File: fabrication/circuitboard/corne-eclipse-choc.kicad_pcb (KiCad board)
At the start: 2 copper layers, 275.5 x 105.6 mm, 178 parts, among them J2 OLED, J4 OLED, SW1 SW_Choc_v1v2_HS, SW10 SW_Choc_v1v2_HS, SW11 SW_Choc_v1v2_HS, SW12 SW_Choc_v1v2_HS, SW13 SW_Choc_v1v2_HS, SW14 SW_Choc_v1v2_HS, SW15 SW_Choc_v1v2_HS, SW16 SW_Choc_v1v2_HS, SW17 SW_Choc_v1v2_HS, SW18 SW_Choc_v1v2_HS, SW2 SW_Choc_v1v2_HS, SW20 SW_Choc_v1v2_HS, SW21 SW_Choc_v1v2_HS, SW22 SW_Choc_v1v2_HS, SW23 SW_Choc_v1v2_HS, SW24 SW_Choc_v1v2_HS, SW25 SW_Choc_v1v2_HS, SW26 SW_Choc_v1v2_HS, SW27 SW_Choc_v1v2_HS, SW28 SW_Choc_v1v2_HS, SW29 SW_Choc_v1v2_HS, SW3 SW_Choc_v1v2_HS, SW30 SW_Choc_v1v2_HS, SW31 SW_Choc_v1v2_HS, SW32 SW_Choc_v1v2_HS, SW33 SW_Choc_v1v2_HS, SW34 SW_Choc_v1v2_HS, SW35 SW_Choc_v1v2_HS, SW36 SW_Choc_v1v2_HS, SW37 SW_Choc_v1v2_HS, SW38 SW_Choc_v1v2_HS, SW39 SW_Choc_v1v2_HS, SW4 SW_Choc_v1v2_HS, SW40 SW_Choc_v1v2_HS, SW42 SW_Choc_v1v2_HS, SW43 SW_Choc_v1v2_HS, SW44 SW_Choc_v1v2_HS, SW5 SW_Choc_v1v2_HS, SW6 SW_Choc_v1v2_HS, SW7 SW_Choc_v1v2_HS, SW8 SW_Choc_v1v2_HS, SW9 SW_Choc_v1v2_HS, U1 nice!nano, U2 nice!nano

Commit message: wip: v3 mx+choc variants
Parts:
- added Q1: AO3401A, Package_TO_SOT_SMD:SOT-23, B.Cu at (123.6, 61.2)
- added Q2: AO3401A, Package_TO_SOT_SMD:SOT-23, B.Cu at (173.2, 61.2)
- added R1: 10k, Resistor_SMD:R_0402_1005Metric, B.Cu at (124.4, 64.0)
- added R2: 10k, Resistor_SMD:R_0402_1005Metric, B.Cu at (172.4, 64.0)
- ENC1, ENC2: value RotaryEncoder_Alps_EC12E-Switch_Vertical_H20mm -> ENC_SW_EC12_Choc; footprint Rotary_Encoder:RotaryEncoder_Alps_EC12E-Switch_Vertical_H20mm -> Corne Eclipse:ENC_SW_EC12_Choc_v1v2_HS_1u
- SW1, SW10, SW11, SW12, SW13, SW14, SW15, SW16, SW17, SW18, SW2, SW20, SW21, SW23, SW24, SW25, SW26, SW27, SW28, SW29, SW3, SW30, SW31, SW32, SW33, SW34, SW35, SW36, SW37, SW38, SW39, SW4, SW40, SW42, SW43, SW5, SW6, SW7, SW8, SW9: footprint corne-eclipse:SW_Choc_v1v2_HS_1u -> Corne Eclipse:SW_Choc_v1v2_HS_1u
- SW22, SW44: footprint corne-eclipse:SW_Choc_v1v2_HS_1.5u -> Corne Eclipse:SW_Choc_v1v2_HS_1.5u
- TP1, TP2: footprint corne-eclipse:Tenting_Puck -> Corne Eclipse:Tenting_Puck
- moved LED36 9.51 mm to (181.6, 65.7), turned to 180 degrees
- moved LED41 9.51 mm to (200.6, 63.3), turned to 180 degrees
- moved LED43 9.51 mm to (210.1, 82.9), turned to 180 degrees
- moved LED44 9.51 mm to (219.6, 60.9), turned to 180 degrees
- moved LED49 9.51 mm to (238.6, 63.3), turned to 180 degrees
- moved LED51 9.51 mm to (257.6, 68.0), turned to 180 degrees
- moved LED56 9.51 mm to (276.6, 68.0), turned to 180 degrees
- moved LED37 9.51 mm to (181.6, 46.7), turned to 180 degrees
- moved LED39 9.51 mm to (200.6, 25.3), turned to 180 degrees
- moved LED40 9.51 mm to (200.6, 44.3), turned to 180 degrees
- moved LED46 9.51 mm to (219.6, 22.9), turned to 180 degrees
- moved LED47 9.51 mm to (238.6, 25.3), turned to 180 degrees
- moved LED48 9.51 mm to (238.6, 44.3), turned to 180 degrees
- moved LED52 9.51 mm to (257.6, 49.0), turned to 180 degrees
- moved LED53 9.51 mm to (257.6, 30.0), turned to 180 degrees
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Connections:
- net Net-(U1-Pad14) renamed SPI_SCK
- net Net-(U2-Pad14) renamed SPI_SCK_r
- LED1 pad 1: VCC -> LED_PWR
- LED1 pad prev: led0-led1 -> LED
- LED10 pad 3: VCC -> LED_PWR
- LED11 pad 3: VCC -> LED_PWR
- LED12 pad 3: VCC -> LED_PWR
- LED13 pad 3: VCC -> LED_PWR
- LED14 pad 3: VCC -> LED_PWR
- LED15 pad 3: VCC -> LED_PWR
- LED16 pad 3: VCC -> LED_PWR
- LED17 pad 3: VCC -> LED_PWR
- LED18 pad 3: VCC -> LED_PWR
- LED19 pad 3: VCC -> LED_PWR
- LED2 pad 1: VCC -> LED_PWR
- LED20 pad 3: VCC -> LED_PWR
- LED21 pad 3: VCC -> LED_PWR
- LED23 pad 3: VCC -> LED_PWR
- LED24 pad 3: VCC -> LED_PWR
- LED25 pad 3: VCC -> LED_PWR
- LED26 pad 3: VCC -> LED_PWR
- LED27 pad 3: VCC -> LED_PWR
- LED28 pad 3: VCC -> LED_PWR
- LED29 pad 1: VDD -> LED_PWR_r
- LED3 pad 1: VCC -> LED_PWR
- LED30 pad 1: VDD -> LED_PWR_r
- LED31 pad 1: VDD -> LED_PWR_r
- LED32 pad 1: VDD -> LED_PWR_r
- LED33 pad 1: VDD -> LED_PWR_r
- LED33B pad 1: VDD -> LED_PWR_r
- LED35 pad 3: VDD -> LED_PWR_r
- LED36 pad 3: VDD -> LED_PWR_r
- LED37 pad 3: VDD -> LED_PWR_r
- LED38 pad 3: VDD -> LED_PWR_r
- LED39 pad 3: VDD -> LED_PWR_r
- LED4 pad 1: VCC -> LED_PWR
- LED40 pad 3: VDD -> LED_PWR_r
- LED41 pad 3: VDD -> LED_PWR_r
- LED42 pad 3: VDD -> LED_PWR_r
- LED43 pad 3: VDD -> LED_PWR_r
- LED44 pad 3: VDD -> LED_PWR_r
- LED45 pad 3: VDD -> LED_PWR_r
- LED46 pad 3: VDD -> LED_PWR_r
- LED47 pad 3: VDD -> LED_PWR_r
- LED48 pad 3: VDD -> LED_PWR_r
- LED49 pad 3: VDD -> LED_PWR_r
- LED5 pad 1: VCC -> LED_PWR
- LED51 pad 3: VDD -> LED_PWR_r
- LED52 pad 3: VDD -> LED_PWR_r
- LED53 pad 3: VDD -> LED_PWR_r
- LED54 pad 3: VDD -> LED_PWR_r
- LED55 pad 3: VDD -> LED_PWR_r
- LED56 pad 3: VDD -> LED_PWR_r
- LED6 pad 1: VCC -> LED_PWR
- LED7 pad 3: VCC -> LED_PWR
- LED8 pad 3: VCC -> LED_PWR
- LED9 pad 3: VCC -> LED_PWR
- U1 pad 13: Net-(U1-Pad13) -> EXT_PWR
- U2 pad 13: Net-(U2-Pad13) -> EXT_PWR_r
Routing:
- net GND: track 0.27 -> 536.8 mm, vias 0 -> 28
- net col0: track 0.00 -> 166.2 mm, vias 0 -> 7
- net row1: track 0.00 -> 150.0 mm, vias 0 -> 4
- net row2: track 0.00 -> 148.5 mm, vias 0 -> 4
- net col2: track 0.00 -> 144.8 mm, vias 0 -> 8
- net col1: track 0.00 -> 140.5 mm, vias 0 -> 3
- net Net-(U1-Pad12): track 0.00 -> 130.6 mm
- net Net-(U1-Pad11): track 0.00 -> 128.4 mm, vias 0 -> 4
- net row0: track 0.00 -> 127.3 mm
- net col3: track 0.00 -> 124.1 mm, vias 0 -> 5
- net row3: track 0.00 -> 110.1 mm
- net col4: track 0.00 -> 101.3 mm, vias 0 -> 8
- net col5: track 0.00 -> 67.1 mm, vias 0 -> 5
- net Net-(U1-Pad24): track 0.00 -> 54.5 mm
- net Net-(D22-Pad2): track 0.00 -> 48.9 mm, vias 0 -> 2
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
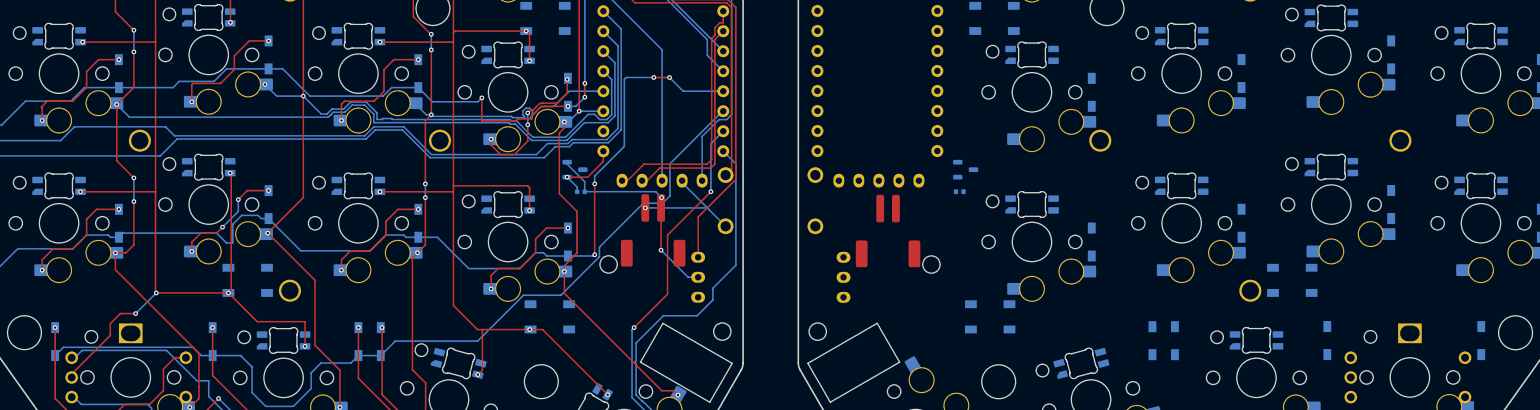
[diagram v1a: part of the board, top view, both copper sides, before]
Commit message: wip: silkscreen, QR codes, plate renames, LED34 cleanup
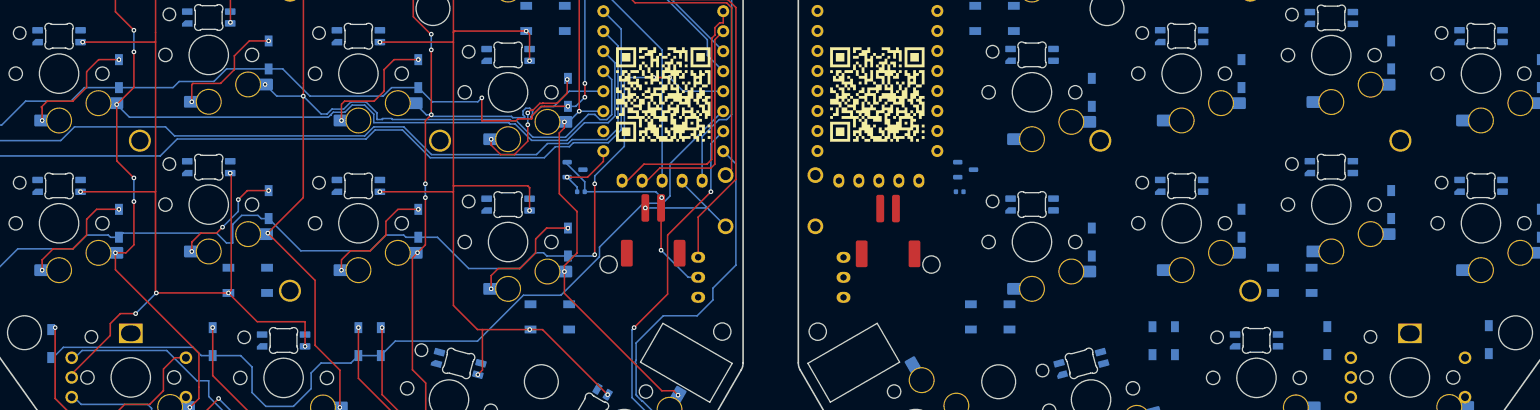
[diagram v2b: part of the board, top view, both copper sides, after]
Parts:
- moved D40B 0.97 mm to (239.6, 82.8)
- moved D19B 0.56 mm to (57.1, 83.3)
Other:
- board text added: "Design by Frosthaven Inspired by foostan's crkbd Choc v1 / v2 Hotswap"

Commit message: wip: logos, silkscreen cleanup, choc shield STLs, diode alignment
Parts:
- moved D24 1.85 mm to (246.2, 28.2)
- moved D13 1.61 mm to (27.7, 71.2)
- moved D3 1.61 mm to (65.7, 28.2)
- moved D4 1.61 mm to (84.7, 26.1)
- moved D5 1.61 mm to (103.7, 28.4)
- moved D1 1.61 mm to (27.7, 33.2)
- moved D10 1.61 mm to (84.7, 45.1)
- moved D11 1.61 mm to (103.7, 47.4)
- moved D12 1.61 mm to (122.7, 49.8)
- moved D14 1.61 mm to (46.7, 71.2)
- moved D15 1.61 mm to (65.7, 66.4)
- moved D16 1.61 mm to (84.7, 64.1)
- moved D17 1.61 mm to (103.7, 66.4)
- moved D18 1.61 mm to (122.7, 68.8)
- moved D2 1.61 mm to (46.7, 33.2)
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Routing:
- net row1: track 150.0 -> 159.7 mm
- net row0: track 127.3 -> 136.8 mm
- net row2: track 148.5 -> 151.2 mm
- net GND: track 536.8 -> 538.8 mm
- net Net-(D12-Pad2): track 18.0 -> 18.9 mm
- net Net-(D7-Pad2): track 14.5 -> 15.1 mm
- net Net-(D5-Pad2): track 14.6 -> 15.2 mm
- net Net-(D2-Pad2): track 14.9 -> 15.6 mm
- net Net-(D1-Pad2): track 14.9 -> 15.6 mm
- net Net-(D9-Pad2): track 15.3 -> 15.9 mm
- net Net-(D8-Pad2): track 14.6 -> 15.3 mm
- net Net-(D4-Pad2): track 14.6 -> 15.2 mm
- net Net-(D3-Pad2): track 14.2 -> 14.9 mm
- net Net-(D18-Pad2): track 15.0 -> 15.6 mm
- net Net-(D16-Pad2): track 14.5 -> 15.2 mm
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
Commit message: wip
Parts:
- moved MH3 0.25 mm to (119.3, 88.4)
- moved MH6 0.25 mm to (177.4, 88.4)
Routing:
- net LED_PWR: track 0.00 -> 471.9 mm, vias 0 -> 25
- net led2-led3: track 0.00 -> 58.0 mm, vias 0 -> 2
- net led13-led14: track 0.00 -> 52.7 mm, vias 0 -> 2
- net led15-led16: track 0.00 -> 52.5 mm, vias 0 -> 4
- net led7-led8: track 0.00 -> 49.1 mm, vias 0 -> 4
- net led24-led25: track 0.00 -> 48.7 mm, vias 0 -> 4
- net led23-led24: track 0.00 -> 48.1 mm, vias 0 -> 2
- net led1-led2: track 0.00 -> 47.2 mm
- net led4-led5: track 0.00 -> 43.8 mm, vias 0 -> 2
- net led8-led9: track 0.00 -> 42.5 mm, vias 0 -> 4
- net led16-led17: track 0.00 -> 37.3 mm, vias 0 -> 2
- net led5-led6: track 0.00 -> 34.0 mm
- net LED: track 0.00 -> 33.2 mm, vias 0 -> 1
- net GND: track 538.8 -> 568.9 mm, vias 28 -> 29
- net led17-led18: track 0.00 -> 29.6 mm, vias 0 -> 2
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
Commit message: feat(pcbs): finished MX/Choc1/Choc2 plates; choc boards
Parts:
- moved SHINE01 9.50 mm to (171.0, 91.8), turned to 120 degrees
- moved R1 0.89 mm to (123.6, 64.5)
- moved R2 0.89 mm to (173.2, 64.5)
- turned RGBMOS to 90 degrees (x2)
- turned SW44 to 120 degrees
- renumbered LED1 to GLOW01, LED29 to GLOW01, LED2 to GLOW02, LED30 to GLOW02, LED3 to GLOW03, LED31 to GLOW03, LED32 to GLOW04, LED4 to GLOW04, LED5 to GLOW05, LED33 to GLOW05, LED6 to GLOW06, LED33B to GLOW06, Q2 to RGBMOS, Q1 to RGBMOS, LED7 to SHINE01, LED35 to SHINE01, LED8 to SHINE02, LED36 to SHINE02, LED9 to SHINE03, LED37 to SHINE03, LED10 to SHINE04, LED38 to SHINE04, LED11 to SHINE05, LED39 to SHINE05, LED12 to SHINE06, LED40 to SHINE06, LED41 to SHINE07, LED13 to SHINE07, LED42 to SHINE08, LED14 to SHINE08, LED43 to SHINE09, LED15 to SHINE09, LED16 to SHINE10, LED44 to SHINE10, LED17 to SHINE11, LED45 to SHINE11, LED18 to SHINE12, LED46 to SHINE12, LED19 to SHINE13, LED47 to SHINE13, LED20 to SHINE14, LED48 to SHINE14, LED21 to SHINE15, LED49 to SHINE15, LED23 to SHINE16, LED51 to SHINE16, LED24 to SHINE17, LED52 to SHINE17, LED25 to SHINE18, LED53 to SHINE18, LED26 to SHINE19, LED54 to SHINE19, LED27 to SHINE20, LED55 to SHINE20, LED28 to SHINE21, LED56 to SHINE21
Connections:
- SW32 pad 1: (no net) -> col3_r
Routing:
- net GNDA: track 0.00 -> 676.3 mm, vias 0 -> 14
- net LED_PWR_r: track 0.00 -> 474.0 mm, vias 0 -> 35
- net col0_r: track 0.00 -> 216.8 mm, vias 0 -> 7
- net col1_r: track 0.00 -> 196.1 mm, vias 0 -> 8
- net row2_r: track 0.00 -> 187.7 mm, vias 0 -> 4
- net col2_r: track 0.00 -> 183.8 mm, vias 0 -> 7
- net row1_r: track 0.00 -> 178.4 mm, vias 0 -> 4
- net col3_r: track 0.00 -> 177.8 mm, vias 0 -> 5
- net row0_r: track 0.00 -> 176.2 mm, vias 0 -> 3
- net col4_r: track 0.00 -> 141.3 mm, vias 0 -> 9
- net col5_r: track 0.00 -> 130.5 mm, vias 0 -> 7
- net row3_r: track 0.00 -> 113.4 mm, vias 0 -> 5
- net Net-(U2-Pad12): track 0.00 -> 102.9 mm, vias 0 -> 1
- net Net-(U2-Pad11): track 0.00 -> 98.9 mm
- net led42-led43: track 0.00 -> 54.3 mm, vias 0 -> 6
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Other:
- board text added: "MOS"
- board text added: "RGB"

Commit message: wip(pcb): better alignment of components on choc pcb
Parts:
- R1, R2: footprint Resistor_SMD:R_0402_1005Metric -> Resistor_SMD:R_1206_3216Metric
- moved GLOW01 50.0 mm to (70.2, 36.5), turned to 90 degrees
- moved GLOW01 50.0 mm to (226.5, 36.5), turned to 90 degrees
- moved D42 37.4 mm to (160.6, 91.9), turned to 30 degrees
- moved D21 36.6 mm to (131.1, 100.6), turned to 150 degrees
- moved GLOW02 30.7 mm to (245.5, 39.5), turned to 90 degrees
- moved GLOW02 30.7 mm to (51.3, 39.5), turned to 90 degrees
- moved D41 19.6 mm to (185.1, 96.1), turned to 105 degrees
- moved GLOW06 16.7 mm to (103.7, 79.3), turned to 90 degrees
- moved GLOW06 16.7 mm to (193.0, 79.3), turned to 90 degrees
- moved D40 16.7 mm to (205.1, 92.0)
- moved GLOW03 16.4 mm to (267.5, 51.7), turned to 90 degrees
- moved GLOW03 16.4 mm to (29.2, 51.7), turned to 90 degrees
- moved D4 16.4 mm to (68.6, 29.0)
- moved D3 16.3 mm to (49.6, 30.5)
- moved D29 15.9 mm to (249.9, 56.3)
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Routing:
- net GNDA: track 676.3 -> 0.00 mm, vias 14 -> 0
- net GND: track 567.9 -> 0.00 mm, vias 29 -> 0
- net LED_PWR_r: track 474.0 -> 0.00 mm, vias 35 -> 0
- net LED_PWR: track 469.9 -> 0.00 mm, vias 25 -> 0
- net col0_r: track 216.8 -> 0.00 mm, vias 7 -> 0
- net col1_r: track 196.1 -> 0.00 mm, vias 8 -> 0
- net row2_r: track 187.7 -> 0.00 mm, vias 4 -> 0
- net col2_r: track 183.8 -> 0.00 mm, vias 7 -> 0
- net row1_r: track 178.4 -> 0.00 mm, vias 4 -> 0
- net col3_r: track 177.8 -> 0.00 mm, vias 5 -> 0
- net row0_r: track 176.2 -> 0.00 mm, vias 3 -> 0
- net col0: track 166.2 -> 0.00 mm, vias 7 -> 0
- net row1: track 159.1 -> 0.00 mm, vias 4 -> 0
- net row2: track 152.9 -> 0.00 mm, vias 4 -> 0
- net col2: track 144.8 -> 0.00 mm, vias 8 -> 0
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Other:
- outline, holes or cut-outs redrawn
- board text removed: "MOS"
- board text removed: "RGB"

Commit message: wip
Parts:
- moved R2 5.01 mm to (171.1, 69.0)
- moved D21 1.35 mm to (130.6, 101.9)
- moved D42 1.28 mm to (159.8, 90.9)
- moved D1 0.79 mm to (14.4, 39.3)
- moved D10 0.79 mm to (71.4, 51.3)
- moved D11 0.79 mm to (90.4, 53.8)
- moved D12 0.79 mm to (109.4, 56.0)
- moved D13 0.79 mm to (14.4, 77.5)
- moved D14 0.79 mm to (33.4, 77.3)
- moved D15 0.79 mm to (52.4, 72.8)
- moved D16 0.79 mm to (71.4, 70.3)
- moved D17 0.79 mm to (90.4, 72.8)
- moved D18 0.79 mm to (109.4, 75.0)
- moved D19 0.79 mm to (80.9, 92.3)
- moved D2 0.79 mm to (33.4, 39.3)
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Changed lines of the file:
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@@
 	(footprint "kbd:D3_SMD_v2"
 		(layer "B.Cu")
-		(at 15.1075 39.005 90)
+		(at 14.3575 39.255 90)
 		(descr "Resitance 3 pas")
 		(tags "R")
@@
 	(footprint "kbd:D3_SMD_v2"
 		(layer "B.Cu")
-		(at 34.1075 39.005 90)
+		(at 33.3575 39.255 90)
 		(descr "Resitance 3 pas")
 		(tags "R")
@@
 	(footprint "kbd:D3_SMD_v2"
 		(layer "B.Cu")
-		(at 91.1075 34.505 90)
+		(at 90.3575 34.755 90)
 		(descr "Resitance 3 pas")
 		(tags "R")
@@
 	(footprint "kbd:D3_SMD_v2"
 		(layer "B.Cu")
-		(at 110.1075 36.755 90)
+		(at 109.3575 37.005 90)
 		(descr "Resitance 3 pas")
 		(tags "R")
@@
 	(footprint "kbd:D3_SMD_v2"
 		(layer "B.Cu")
-		(at 15.1075 58.255 90)
+		(at 14.3575 58.505 90)
 		(descr "Resitance 3 pas")
 		(tags "R")
@@
 	(footprint "kbd:D3_SMD_v2"
 		(layer "B.Cu")
-		(at 34.1075 58.255 90)
+		(at 33.3575 58.505 90)
 		(descr "Resitance 3 pas")
 		(tags "R")
@@
 	(footprint "kbd:D3_SMD_v2"
 		(layer "B.Cu")
-		(at 53.1075 53.505 90)
+		(at 52.3575 53.755 90)
 		(descr "Resitance 3 pas")
 		(tags "R")
@@
 	(footprint "kbd:D3_SMD_v2"
 		(layer "B.Cu")
-		(at 72.1075 51.055 90)
+		(at 71.3575 51.305 90)
 		(descr "Resitance 3 pas")
 		(tags "R")
@@
 	(footprint "kbd:D3_SMD_v2"
 		(layer "B.Cu")
-		(at 91.1075 53.505 90)
+		(at 90.3575 53.755 90)
 		(descr "Resitance 3 pas")
 		(tags "R")
@@
 	(footprint "kbd:D3_SMD_v2"
 		(layer "B.Cu")
-		(at 110.1075 55.755 90)
+		(at 109.3575 56.005 90)
 		(descr "Resitance 3 pas")
 		(tags "R")
@@
 	(footprint "kbd:D3_SMD_v2"
 		(layer "B.Cu")
-		(at 15.1075 77.255 90)
+		(at 14.3575 77.505 90)
 		(descr "Resitance 3 pas")
 		(tags "R")
@@
 	(footprint "kbd:D3_SMD_v2"
 		(layer "B.Cu")
-		(at 34.1075 77.005 90)
+		(at 33.3575 77.255 90)
 		(descr "Resitance 3 pas")
 		(tags "R")
@@
 	(footprint "kbd:D3_SMD_v2"
 		(layer "B.Cu")
-		(at 53.1075 72.505 90)
+		(at 52.3575 72.755 90)
 		(descr "Resitance 3 pas")
 		(tags "R")
@@
 	(footprint "kbd:D3_SMD_v2"
 		(layer "B.Cu")
-		(at 72.1075 70.005 90)
+		(at 71.3575 70.255 90)
 		(descr "Resitance 3 pas")
 		(tags "R")
@@
 	(footprint "kbd:D3_SMD_v2"
 		(layer "B.Cu")
-		(at 91.1075 72.505 90)
+		(at 90.3575 72.755 90)
 		(descr "Resitance 3 pas")
 		(tags "R")
@@
 	(footprint "kbd:D3_SMD_v2"
 		(layer "B.Cu")
-		(at 110.1075 74.755 90)
+		(at 109.3575 75.005 90)
 		(descr "Resitance 3 pas")
 		(tags "R")
@@
 	(footprint "kbd:D3_SMD_v2"
 		(layer "B.Cu")
-		(at 81.6075 92.005 90)
+		(at 80.8575 92.255 90)
 		(descr "Resitance 3 pas")
 		(tags "R")
@@
 	(footprint "kbd:D3_SMD_v2"
 		(layer "B.Cu")
-		(at 101.566904 93.315482 75)
+		(at 100.816904 93.315482 75)
 		(descr "Resitance 3 pas")
 		(tags "R")
@@
 	(footprint "kbd:D3_SMD_v2"
 		(layer "B.Cu")
-		(at 131.070305 100.6425 150)
+		(at 130.570305 101.8925 150)
 		(descr "Resitance 3 pas")
 		(tags "R")
@@
 	(footprint "kbd:D3_SMD_v2"
 		(layer "B.Cu")
-		(at 252.6075 39.005 90)
+		(at 251.8575 39.255 90)
 		(descr "Resitance 3 pas")
 		(tags "R")
@@
 	(footprint "kbd:D3_SMD_v2"
 		(layer "B.Cu")
-		(at 233.6075 34.305 90)
+		(at 232.8575 34.555 90)
 		(descr "Resitance 3 pas")
 		(tags "R")
@@
 	(footprint "kbd:D3_SMD_v2"
 		(layer "B.Cu")
-		(at 214.6075 32.005 90)
+		(at 213.8575 32.255 90)
 		(descr "Resitance 3 pas")
 		(tags "R")
@@
 	(footprint "kbd:D3_SMD_v2"
 		(layer "B.Cu")
-		(at 176.6075 36.805 90)
+		(at 175.8575 37.055 90)
 		(descr "Resitance 3 pas")
 		(tags "R")
@@
 	(footprint "kbd:D3_SMD_v2"
 		(layer "B.Cu")
-		(at 271.6075 58.005 90)
+		(at 270.8575 58.255 90)
 		(descr "Resitance 3 pas")
 		(tags "R")
@@
 	(footprint "kbd:D3_SMD_v2"
 		(layer "B.Cu")
-		(at 249.8575 56.255 90)
+		(at 249.1075 56.505 90)
 		(descr "Resitance 3 pas")
 		(tags "R")
@@
 	(footprint "kbd:D3_SMD_v2"
 		(layer "B.Cu")
-		(at 214.6075 51.005 90)
+		(at 213.8575 51.255 90)
 		(descr "Resitance 3 pas")
 		(tags "R")
@@
 	(footprint "kbd:D3_SMD_v2"
 		(layer "B.Cu")
-		(at 195.6075 53.505 90)
+		(at 194.8575 53.755 90)
 		(descr "Resitance 3 pas")
 		(tags "R")
@@
 	(footprint "kbd:D3_SMD_v2"
 		(layer "B.Cu")
-		(at 176.6075 55.755 90)
+		(at 175.8575 56.005 90)
 		(descr "Resitance 3 pas")
 		(tags "R")
@@
 	(footprint "kbd:D3_SMD_v2"
 		(layer "B.Cu")
-		(at 271.6075 77.005 90)
+		(at 270.8575 77.255 90)
 		(descr "Resitance 3 pas")
 		(tags "R")
@@
 	(footprint "kbd:D3_SMD_v2"
 		(layer "B.Cu")
-		(at 252.6075 77.005 90)
+		(at 251.8575 77.255 90)
 		(descr "Resitance 3 pas")
 		(tags "R")
@@
 	(footprint "kbd:D3_SMD_v2"
 		(layer "B.Cu")
-		(at 233.6075 72.255 90)
+		(at 232.8575 72.505 90)
 		(descr "Resitance 3 pas")
 		(tags "R")
@@
 	(footprint "kbd:D3_SMD_v2"
 		(layer "B.Cu")
-		(at 214.6075 70.005 90)
+		(at 213.8575 70.255 90)
 		(descr "Resitance 3 pas")
 		(tags "R")
@@
 	(footprint "kbd:D3_SMD_v2"
 		(layer "B.Cu")
-		(at 195.6075 72.505 90)
+		(at 194.8575 72.755 90)
 		(descr "Resitance 3 pas")
 		(tags "R")
@@
 	(footprint "kbd:D3_SMD_v2"
 		(layer "B.Cu")
-		(at 176.6075 74.755 90)
+		(at 175.8575 75.005 90)
 		(descr "Resitance 3 pas")
 		(tags "R")
@@
 	(footprint "kbd:D3_SMD_v2"
 		(layer "B.Cu")
-		(at 205.1075 92.005 90)
+		(at 204.3575 92.255 90)
 		(descr "Resitance 3 pas")
 		(tags "R")
@@
 	(footprint "kbd:D3_SMD_v2"
 		(layer "B.Cu")
-		(at 185.148096 96.065482 105)
+		(at 184.398096 96.315482 105)
 		(descr "Resitance 3 pas")
 		(tags "R")
@@
 	(footprint "kbd:D3_SMD_v2"
 		(layer "B.Cu")
-		(at 160.644695 91.8925 30)
+		(at 159.820305 90.9175 30)
 		(descr "Resitance 3 pas")
 		(tags "R")
@@
 	(footprint "kbd:D3_SMD_v2"
 		(layer "B.Cu")
-		(at 271.6075 39.255 90)
+		(at 270.8575 39.505 90)
 		(descr "Resitance 3 pas")
 		(tags "R")
@@
 	(footprint "kbd:D3_SMD_v2"
 		(layer "B.Cu")
-		(at 195.6075 34.505 90)
+		(at 194.8575 34.755 90)
 		(descr "Resitance 3 pas")
 		(tags "R")
@@
 	(footprint "Resistor_SMD:R_1206_3216Metric"
 		(layer "B.Cu")
-		(at 173.1525 64.5 180)
+		(at 171.0625 69.05 180)
 		(descr "10k Pull-up Resistor for MOSFET Gate")
 		(tags "resistor 1206")
